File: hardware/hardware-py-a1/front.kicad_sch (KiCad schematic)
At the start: 27 parts, among them J3 LCD_socket, J4 Micro_SD_Card_Det2, J5 AudioJack4, Q8 BSS138, Q9 BSS138

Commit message: hw: fixes for py-a1
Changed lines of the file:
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@@
+		)
+	)
+	(hierarchical_label "GND"
+		(shape input)
+		(at 105.41 39.37 0)
+		(effects
+			(font
+				(size 1.27 1.27)
+			)
+			(justify left)
 		)
 	)
@@
 			)
 			(justify left)
+		)
+	)
+	(hierarchical_label "GND"
+		(shape input)
+		(at 208.28 85.09 270)
+		(effects
+			(font
+				(size 1.27 1.27)
+			)
+			(justify right)
 		)
 	)
@@
 					(unit 1)
 				)
-			)
-		)
-	)
-	(symbol
-		(lib_id "power:GND")
-		(at 208.28 85.09 0)
-		(mirror y)
-		(unit 1)
-		(exclude_from_sim no)
-		(in_bom yes)
-		(on_board yes)
-		(dnp no)
-		(property "Reference" "#PWR023"
-			(at 208.28 91.44 0)
-			(effects
-				(font
-					(size 1.27 1.27)
-				)
-				(hide yes)
-			)
-		)
-		(property "Value" "GND"
-			(at 208.28 88.392 0)
-			(effects
-				(font
-					(size 1.27 1.27)
-				)
-			)
-		)
-		(property "Footprint" ""
-			(at 208.28 85.09 0)
-			(effects
-				(font
-					(size 1.27 1.27)
-				)
-				(hide yes)
-			)
-		)
-		(property "Datasheet" ""
-			(at 208.28 85.09 0)
-			(effects
-				(font
-					(size 1.27 1.27)
-				)
-				(hide yes)
-			)
-		)
-		(property "Description" "Power symbol creates a global label with name \"GND\" , ground"
-			(at 208.28 85.09 0)
-			(effects
-				(font
-					(size 1.27 1.27)
-				)
-				(hide yes)
-			)
-		)
-		(pin "1"
-		)
-		(instances
-			(project "numcalcium"
-				(path "/842c0813-91d3-4f68-bc1f-ac3ce07be478/88d65574-4a55-44b9-b6d2-8e7d5a1c096b"
-					(reference "#PWR023")
-					(unit 1)
-				)

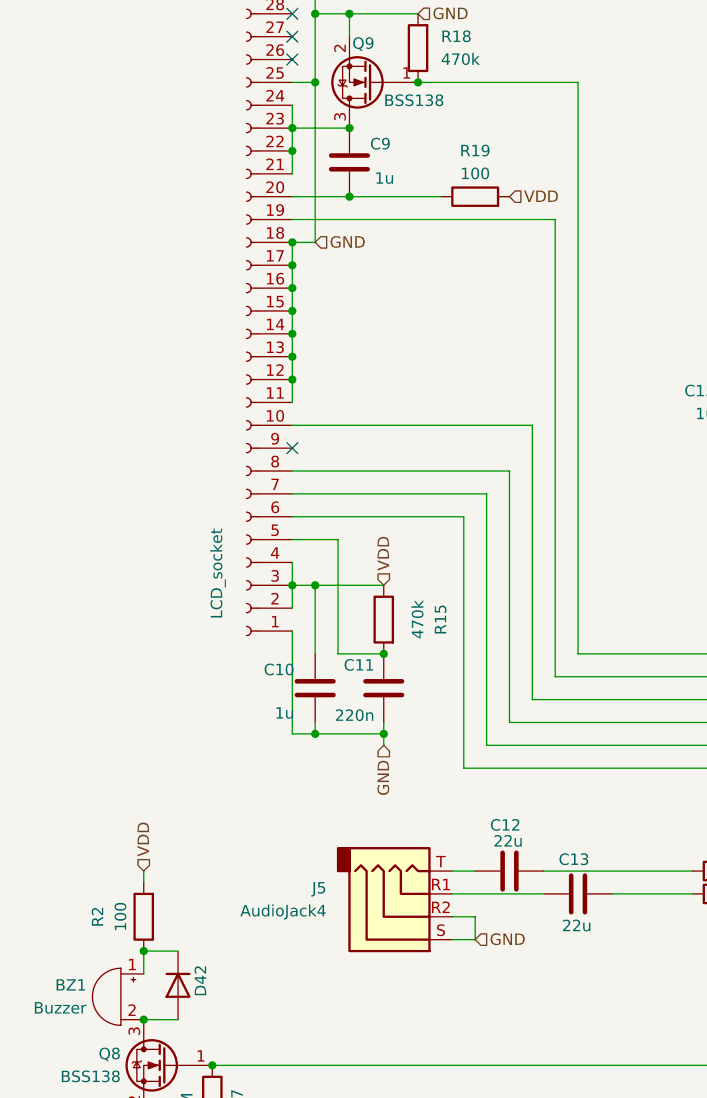
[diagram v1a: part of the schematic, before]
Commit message: hw: pya1 schematic rearange and post assembly test for inputs
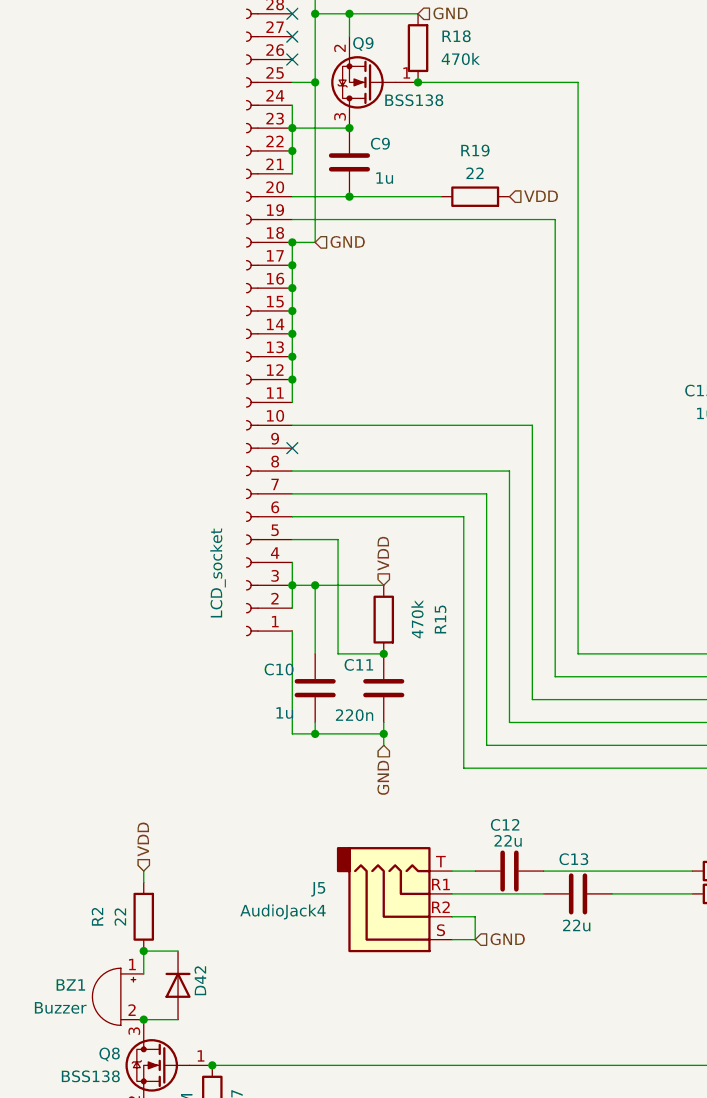
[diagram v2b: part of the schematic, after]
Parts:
- R19, R2: value 100 -> 22
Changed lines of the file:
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@@
 			)
 		)
-		(property "Value" "100"
+		(property "Value" "22"
 			(at 111.76 57.15 90)
 			(effects
@@
 			)
 		)
-		(property "Value" "100"
+		(property "Value" "22"
 			(at 72.39 139.7 90)
 			(effects
